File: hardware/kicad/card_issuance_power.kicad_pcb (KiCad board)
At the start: 2 copper layers, 124.5 x 132.5 mm, 39 parts, among them J1 V12_IN, J2 V12_OUT, J3 V3V3_OUT, J4 V5.1_OUT, Q1 IRF4905, U1 PTSM82903SISB2R, U2 LMZ23610TZ/NOPB

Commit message: feat: added settings - pcb design
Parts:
- moved TP1 69.7 mm to (128.6, 34.2)
- moved F1 63.8 mm to (124.0, 55.2)
- moved R1 61.1 mm to (122.5, 34.2), turned to 0 degrees
- moved J1 60.2 mm to (111.5, 37.2), turned to 0 degrees
- moved R5 58.6 mm to (122.5, 50.4)
- moved R4 52.0 mm to (122.5, 46.4)
- moved U2 39.1 mm to (107.4, 104.6)
- moved J2 37.8 mm to (111.5, 46.9)
- moved U1 28.3 mm to (140.7, 87.6)
- moved C2 21.8 mm to (128.2, 42.3)
- moved R3 21.8 mm to (122.5, 42.3)
- moved C1 21.8 mm to (95.9, 39.2)
- moved C10 21.8 mm to (125.6, 98.5)
- moved C11 21.8 mm to (125.6, 103.0)
- moved C12 21.8 mm to (100.7, 81.9)
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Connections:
- net /BUCK_3V3/VIN renamed /V12_PROT_5V
- net /BUCK_3V3/VOUT renamed /V3V3_OUT
- net /BUCK_5.1/VOUT renamed /V5.1_OUT
- net Net-(D1-A) renamed /V12_FUSED
- net Net-(J1-Pin_1) renamed /V12_IN
- net Net-(J1-Pin_2) renamed /GND_STAR
- net Net-(J2-Pin_1) renamed /V12_PROT_12V
- net Net-(Q1-D) renamed /V12_PROT
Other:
- board outline removed
- copper layers 2 -> 4

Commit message: chore: pcb board components placements
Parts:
- moved R2 87.9 mm to (181.2, 103.7)
- moved R3 87.9 mm to (181.2, 107.8)
- moved R1 86.3 mm to (152.0, 115.3), turned to 90 degrees
- moved R4 84.1 mm to (170.7, 115.2)
- moved TP2 69.9 mm to (58.8, 38.5), turned to 90 degrees
- moved C9 62.1 mm to (125.8, 44.5), turned to 90 degrees
- moved F1 61.3 mm to (69.5, 27.1), turned to -90 degrees
- moved TP1 60.8 mm to (69.2, 21.2), turned to 90 degrees
- moved J3 59.2 mm to (60.3, 86.3), turned to -90 degrees
- moved C8 57.8 mm to (120.8, 44.5), turned to 90 degrees
- moved Q1 57.6 mm to (80.8, 34.3), turned to 180 degrees
- moved C4 57.5 mm to (129.8, 113.8), turned to -90 degrees
- moved C7 53.9 mm to (115.5, 44.5), turned to 90 degrees
- moved R5 53.5 mm to (69.0, 48.2), turned to 180 degrees
- moved J1 51.9 mm to (60.6, 27.3), turned to -90 degrees
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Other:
- board outline added: 158 x 114.5 mm

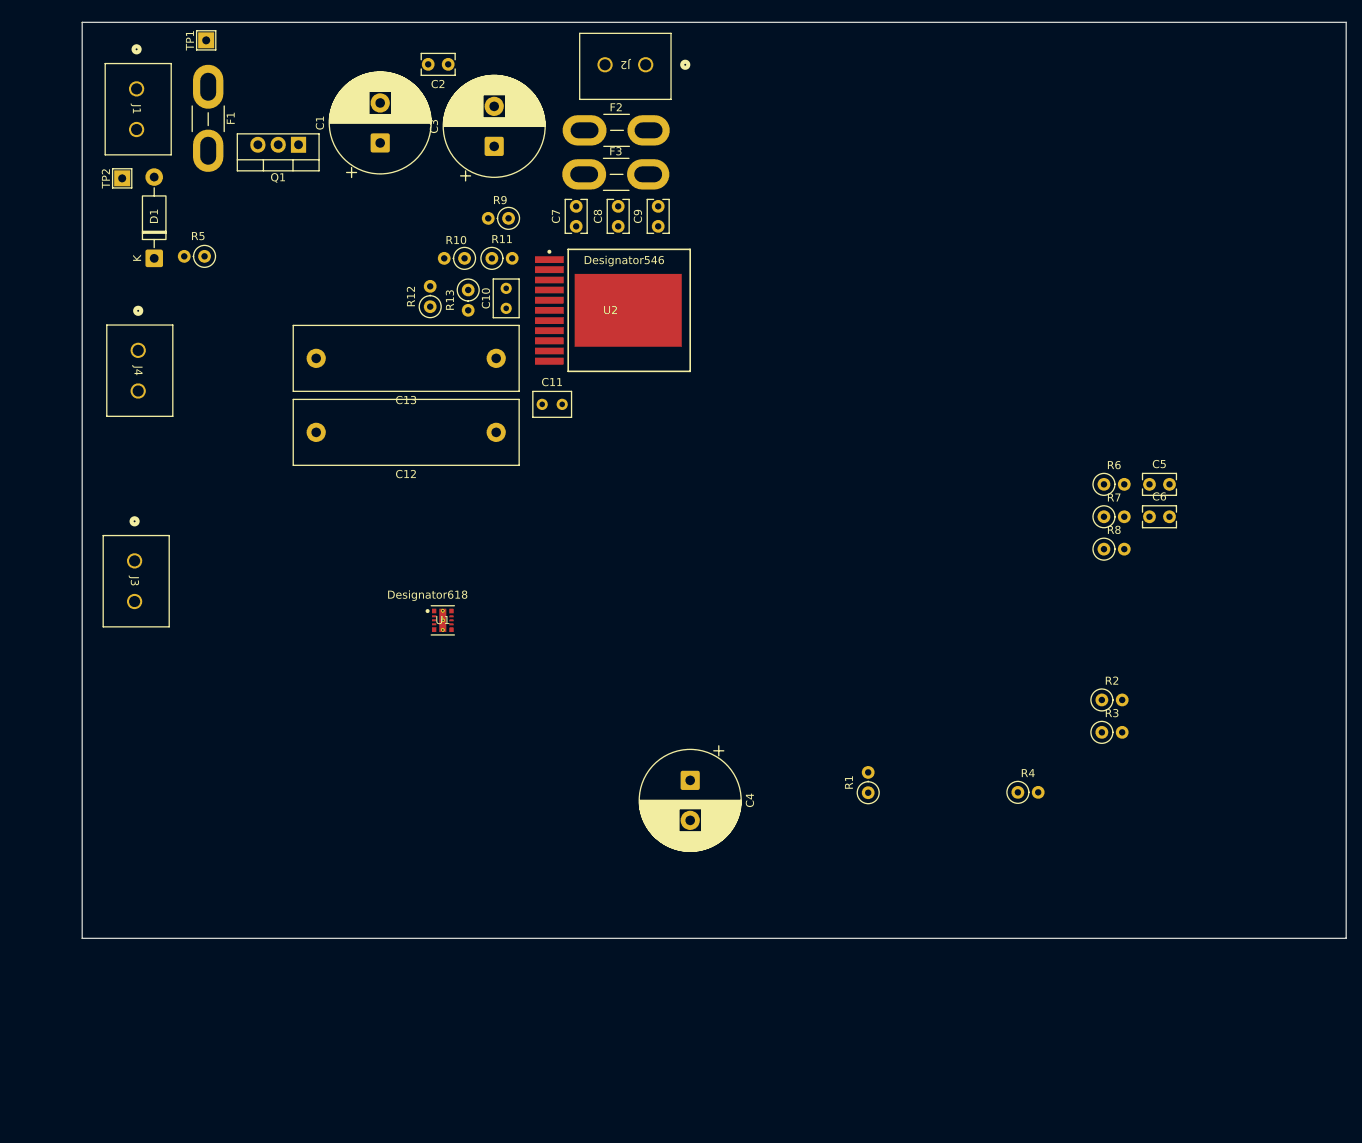
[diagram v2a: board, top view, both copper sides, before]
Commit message: chore: pcb planes filling & vias
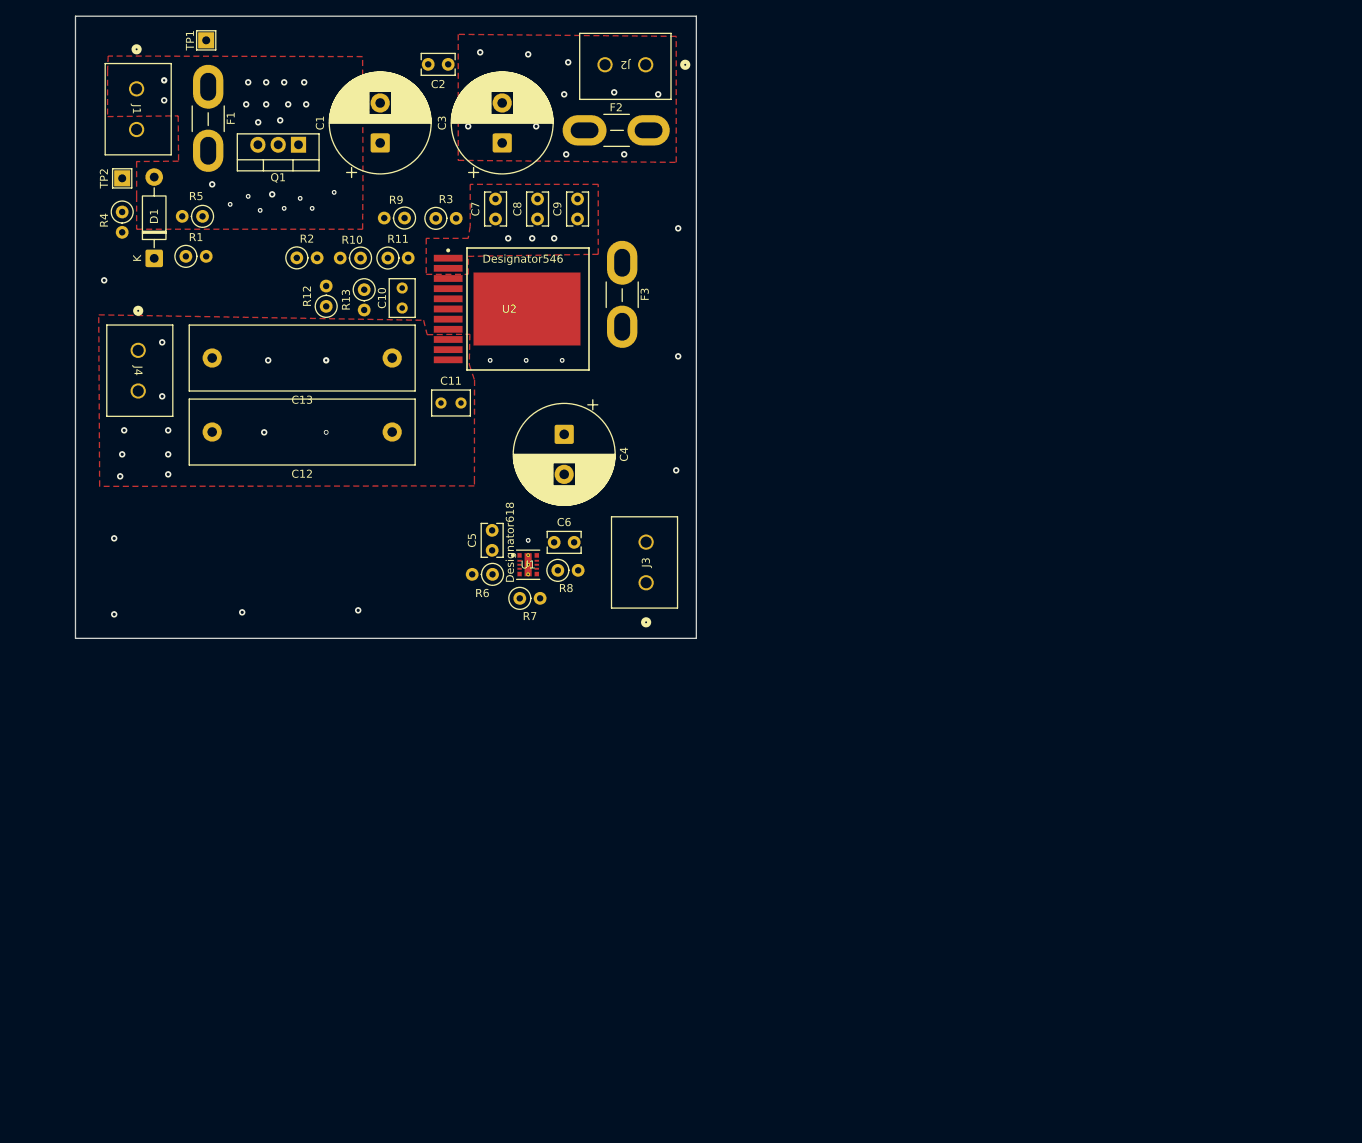
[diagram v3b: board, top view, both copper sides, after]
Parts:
- moved R4 133.4 mm to (58.8, 42.7), turned to -90 degrees
- moved R2 114.8 mm to (80.6, 48.4)
- moved R1 108.5 mm to (66.7, 48.2), turned to 0 degrees
- moved R3 105.2 mm to (98.0, 43.5)
- moved C5 82.6 mm to (105.0, 85.0), turned to 90 degrees
- moved R6 77.3 mm to (105.0, 88.0), turned to 180 degrees
- moved C6 74.5 mm to (112.7, 84.0)
- moved R7 73.7 mm to (108.5, 91.0)
- moved R8 68.3 mm to (113.2, 87.5)
- moved J3 64.0 mm to (124.2, 89.0), turned to 90 degrees
- moved C4 46.0 mm to (114.0, 70.5)
- moved C10 13.0 mm to (93.8, 52.2)
- moved C12 13.0 mm to (92.5, 70.2)
- moved C13 13.0 mm to (92.5, 61.0)
- moved R10 13.0 mm to (88.5, 48.5)
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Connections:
- F3 pad 2: /GND_LOGIC -> /V12_PROT_5V
- TP1 pad 1: /V12_IN -> /V12_FUSED
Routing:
- net /V5.1_OUT: vias 0 -> 12
- net /V12_PROT_5V: vias 0 -> 3
- net /V12_PROT_12V: vias 0 -> 10
- net /V12_IN: vias 0 -> 21
- net /GND_STAR: vias 0 -> 8
- net (no net): vias 0 -> 4
- added copper zone on In1.Cu, net /GND_STAR
- added copper zone on F.Cu, net /V12_IN
- added copper zone on In2.Cu, net /V12_IN
- added copper zone on F.Cu, net /V12_PROT_12V
- added copper zone on In2.Cu, net /V12_PROT_12V
- added copper zone on F.Cu, net /V12_PROT_5V
- added copper zone on In2.Cu, net /V3V3_OUT
- added copper zone on F.Cu, net /V5.1_OUT
- added copper zone on In2.Cu, net /V5.1_OUT
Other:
- board size 158 x 114.5 mm -> 77.6 x 77.8 mm

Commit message: feat: added motor driver circuit
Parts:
- removed C1, C3, C4: 470uF, Capacitor_THT:CP_Radial_D12.5mm_P5.00mm
- removed C10: 0.47uF, Capacitor_THT:C_Rect_L4.6mm_W3.0mm_P2.50mm_MKS02_FKP02
- removed C11: 4.7nF, Capacitor_THT:C_Rect_L4.6mm_W3.0mm_P2.50mm_MKS02_FKP02
- removed C12, C13: 330uF, Capacitor_THT:C_Rect_L28.0mm_W8.0mm_P22.50mm_MKS4
- removed C2: 100nF, Capacitor_THT:C_Rect_L4.0mm_W2.5mm_P2.50mm
- removed C5, C7, C8, C9: 10uF, Capacitor_THT:C_Rect_L4.0mm_W2.5mm_P2.50mm
- removed C6: 22uF, Capacitor_THT:C_Rect_L4.0mm_W2.5mm_P2.50mm
- removed D1: 15V, Diode_THT:D_DO-41_SOD81_P10.16mm_Horizontal
- removed F1, F2, F3: Fuse, Fuse:Fuse_Blade_Mini_directSolder
- removed J1: V12_IN, Terminals:CONN_PM 5.08&slash_02&slash_90 3.5SN BK BX_WED
- removed J2: V12_OUT, Terminals:CONN_PM 5.08&slash_02&slash_90 3.5SN BK BX_WED
- removed J3: V3V3_OUT, Terminals:CONN_PM 5.08&slash_02&slash_90 3.5SN BK BX_WED
- removed J4: V5.1_OUT, Terminals:CONN_PM 5.08&slash_02&slash_90 3.5SN BK BX_WED
- removed Q1: IRF4905, Package_TO_SOT_THT:TO-220-3_Vertical
- removed R1, R4: 100k, Resistor_THT:R_Axial_DIN0207_L6.3mm_D2.5mm_P2.54mm_Vertical
- removed R10, R7: 10k, Resistor_THT:R_Axial_DIN0207_L6.3mm_D2.5mm_P2.54mm_Vertical
- removed R11: 100R, Resistor_THT:R_Axial_DIN0207_L6.3mm_D2.5mm_P2.54mm_Vertical
- removed R12: 5.49k, Resistor_THT:R_Axial_DIN0207_L6.3mm_D2.5mm_P2.54mm_Vertical
- removed R13: 1k, Resistor_THT:R_Axial_DIN0207_L6.3mm_D2.5mm_P2.54mm_Vertical
- removed R2, R3: 0R, Resistor_THT:R_Axial_DIN0207_L6.3mm_D2.5mm_P2.54mm_Vertical
- removed R5: 220R, Resistor_THT:R_Axial_DIN0207_L6.3mm_D2.5mm_P2.54mm_Vertical
- removed R6: 32.4k, Resistor_THT:R_Axial_DIN0207_L6.3mm_D2.5mm_P2.54mm_Vertical
- removed R8: 251k, Resistor_THT:R_Axial_DIN0207_L6.3mm_D2.5mm_P2.54mm_Vertical
- removed R9: 48k, Resistor_THT:R_Axial_DIN0207_L6.3mm_D2.5mm_P2.54mm_Vertical
- removed TP1: V12_IN, TestPoint:TestPoint_THTPad_2.0x2.0mm_Drill1.0mm
- removed TP2: GND, TestPoint:TestPoint_THTPad_2.0x2.0mm_Drill1.0mm
- removed U1: PTSM82903SISB2R, Buck 3V3:SIS0011A-MFG
- removed U2: LMZ23610TZ/NOPB, Buck 5V:NDY0011A_N
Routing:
- net /V5.1_OUT: vias 12 -> 0
- net /V12_PROT_5V: vias 3 -> 0
- net /V12_PROT_12V: vias 10 -> 0
- net /V12_IN: vias 21 -> 0
- net /GND_STAR: vias 8 -> 0
- net (no net): vias 4 -> 0
- removed copper zone on F.Cu, net /V12_IN
- removed copper zone on F.Cu, net /V12_PROT_12V
- removed copper zone on F.Cu, net /V12_PROT_5V
- removed copper zone on F.Cu, net /V5.1_OUT
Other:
- board outline removed
